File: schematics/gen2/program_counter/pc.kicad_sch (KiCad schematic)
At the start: 16 parts, among them J1 Bus_PCI_Express_x16, U1 74LS00, U2 74LS193, U3 74LS193, U4 74LS193, U5 74LS193, U6 74LS245, U7 74LS245

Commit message: pc and sp sch
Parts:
- removed C1, C2, C3, C4, C5, C6, C7, C8: C, Capacitor_THT:CP_Radial_D4.0mm_P1.50mm, symbol Device:C
- removed J1: Bus_PCI_Express_x16, Connector_PCBEdge:BUS_PCIexpress_x16, symbol Connector:Bus_PCI_Express_x16
- removed U1: 74LS00, Package_DIP:DIP-14_W7.62mm_Socket_LongPads, symbol 74xx:74LS00
- removed U2, U3, U4, U5: 74LS193, Package_DIP:DIP-16_W7.62mm_Socket_LongPads, symbol 74xx:74LS193
- removed U6, U7: 74LS245, Package_DIP:DIP-20_W7.62mm_Socket_LongPads, symbol 74xx:74LS245
- added BC1: BusConnector, Connector_PCBEdge:BUS_PCIexpress_x16, symbol cpu816symbols:BusConnector
- added C10, C11, C12, C13, C14, C15, C16, C9: C, Capacitor_THT:CP_Radial_D4.0mm_P1.50mm, symbol Device:C
- added U1: 74HC00, Package_DIP:DIP-14_W7.62mm_Socket_LongPads, symbol 74xx:74HC00
- added U2, U3, U4, U5: 74HC193, Package_DIP:DIP-16_W7.62mm_Socket_LongPads, symbol 74xx:74HC193
- added U6, U7: 74HC245, Package_DIP:DIP-20_W7.62mm_Socket_LongPads, symbol 74xx:74HC245
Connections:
- net CPu: now also U1.3, U4.5 (UP)
- net DH0: now also U2.3 (QA), U7.18 (B0)
- net DH1: now also U2.2 (QB), U7.17 (B1)
- net DH2: now also U2.6 (QC), U7.16 (B2)
- net DH3: now also U2.7 (QD), U7.15 (B3)
- net DH4: now also U3.3 (QA), U7.14 (B4)
- net DH5: now also U3.2 (QB), U7.13 (B5)
- net DH6: now also U3.6 (QC), U7.12 (B6)
- net DH7: now also U3.7 (QD), U7.11 (B7)
- net DL0: now also U4.3 (QA), U6.18 (B0)
- net DL1: now also U4.2 (QB), U6.17 (B1)
- net DL2: now also U4.6 (QC), U6.16 (B2)
- net DL3: now also U4.7 (QD), U6.15 (B3)
- net DL4: now also U5.3 (QA), U6.14 (B4)
- net DL5: now also U5.2 (QB), U6.13 (B5)
- net DL6: now also U5.6 (QC), U6.12 (B6)
- net DL7: now also U5.7 (QD), U6.11 (B7)
- net GND: now also BC1.A12 (GND), BC1.A13 (GND), BC1.A23 (GND), BC1.A32 (GND), BC1.A41 (GND), BC1.A50 (GND), BC1.A59 (GND), BC1.A63 (GND), BC1.A64 (GND), BC1.A65 (GND), BC1.A66 (GND), BC1.A70 (GND), BC1.A71 (GND), BC1.A72 (GND), BC1.A73 (GND), BC1.A74 (GND), BC1.A75 (GND), BC1.A76 (GND), BC1.B12 (GND), BC1.B13 (GND), BC1.B23 (GND), BC1.B32 (GND), BC1.B41 (GND), BC1.B50 (GND), BC1.B59 (GND), BC1.B62 (GND), BC1.B63 (GND), BC1.B64 (GND), BC1.B65 (GND), BC1.B66 (GND), BC1.B67 (GND), BC1.B68 (GND), BC1.B69 (GND), BC1.B70 (GND), BC1.B71 (GND), BC1.B72 (GND), BC1.B75 (GND), BC1.B76 (GND), C10.1, C11.1, C12.1, C13.1, C14.1, C15.2, C16.2, C9.2, U1.7 (GND), U2.8 (GND), U3.8 (GND), U4.8 (GND), U5.8 (GND), U6.1 (A->B), U6.10 (GND), U7.1 (A->B), U7.10 (GND)
- net PULSE: now also BC1.B74 (PULSE), U1.10, U1.13
- net Ph: now also U1.8, U2.11 (~{LOAD}), U3.11 (~{LOAD})
- net Pl: now also U1.11, U4.11 (~{LOAD}), U5.11 (~{LOAD})
- net VCC: now also BC1.A1 (VCC), BC1.A2 (VCC), BC1.A3 (VCC), BC1.A4 (VCC), BC1.A5 (VCC), BC1.B1 (VCC), BC1.B2 (VCC), BC1.B3 (VCC), BC1.B4 (VCC), BC1.B5 (VCC), C10.2, C11.2, C12.2, C13.2, C14.2, C15.1, C16.1, C9.1, U1.14 (VCC), U2.16 (VCC), U3.16 (VCC), U4.16 (VCC), U5.16 (VCC), U6.20 (VCC), U7.20 (VCC)
- new net: U2.12 (~{CO}), U3.5 (UP)
- new net: U2.13 (~{BO}), U3.4 (DOWN)
- new net: U2.4 (DOWN), U5.13 (~{BO})
- new net: U2.5 (UP), U5.12 (~{CO})
- new net: U4.12 (~{CO}), U5.5 (UP)
- new net: U4.13 (~{BO}), U5.4 (DOWN)
- new net DATA0: BC1.A51 (DATA0), U2.15 (A), U4.15 (A), U6.2 (A0), U7.2 (A0)
- new net DATA1: BC1.A52 (DATA1), U2.1 (B), U4.1 (B), U6.3 (A1), U7.3 (A1)
- new net DATA2: BC1.A53 (DATA2), U2.10 (C), U4.10 (C), U6.4 (A2), U7.4 (A2)
- new net DATA3: BC1.A54 (DATA3), U2.9 (D), U4.9 (D), U6.5 (A3), U7.5 (A3)
- new net DATA4: BC1.A55 (DATA4), U3.15 (A), U5.15 (A), U6.6 (A4), U7.6 (A4)
- new net DATA5: BC1.A56 (DATA5), U3.1 (B), U5.1 (B), U6.7 (A5), U7.7 (A5)
- new net DATA6: BC1.A57 (DATA6), U3.10 (C), U5.10 (C), U6.8 (A6), U7.8 (A6)
- new net DATA7: BC1.A58 (DATA7), U3.9 (D), U5.9 (D), U6.9 (A7), U7.9 (A7)
- new net LPCH: BC1.A17 (LPCH), U1.9
- new net LPCL: BC1.A18 (LPCL), U1.12
- new net PCINC: BC1.B47 (PCINC), U1.1
- new net RESET: BC1.A69 (RESET), U2.14 (CLR), U3.14 (CLR), U4.14 (CLR), U5.14 (CLR)
- new net ~{CLK}: BC1.B73 (~{CLK}), U1.2
- new net ~{RPCH}: BC1.B17 (~{RPCH}), U7.19 (CE)
- new net ~{RPCL}: BC1.B18 (~{RPCL}), U6.19 (CE)
- no-connect marks 4 -> 82

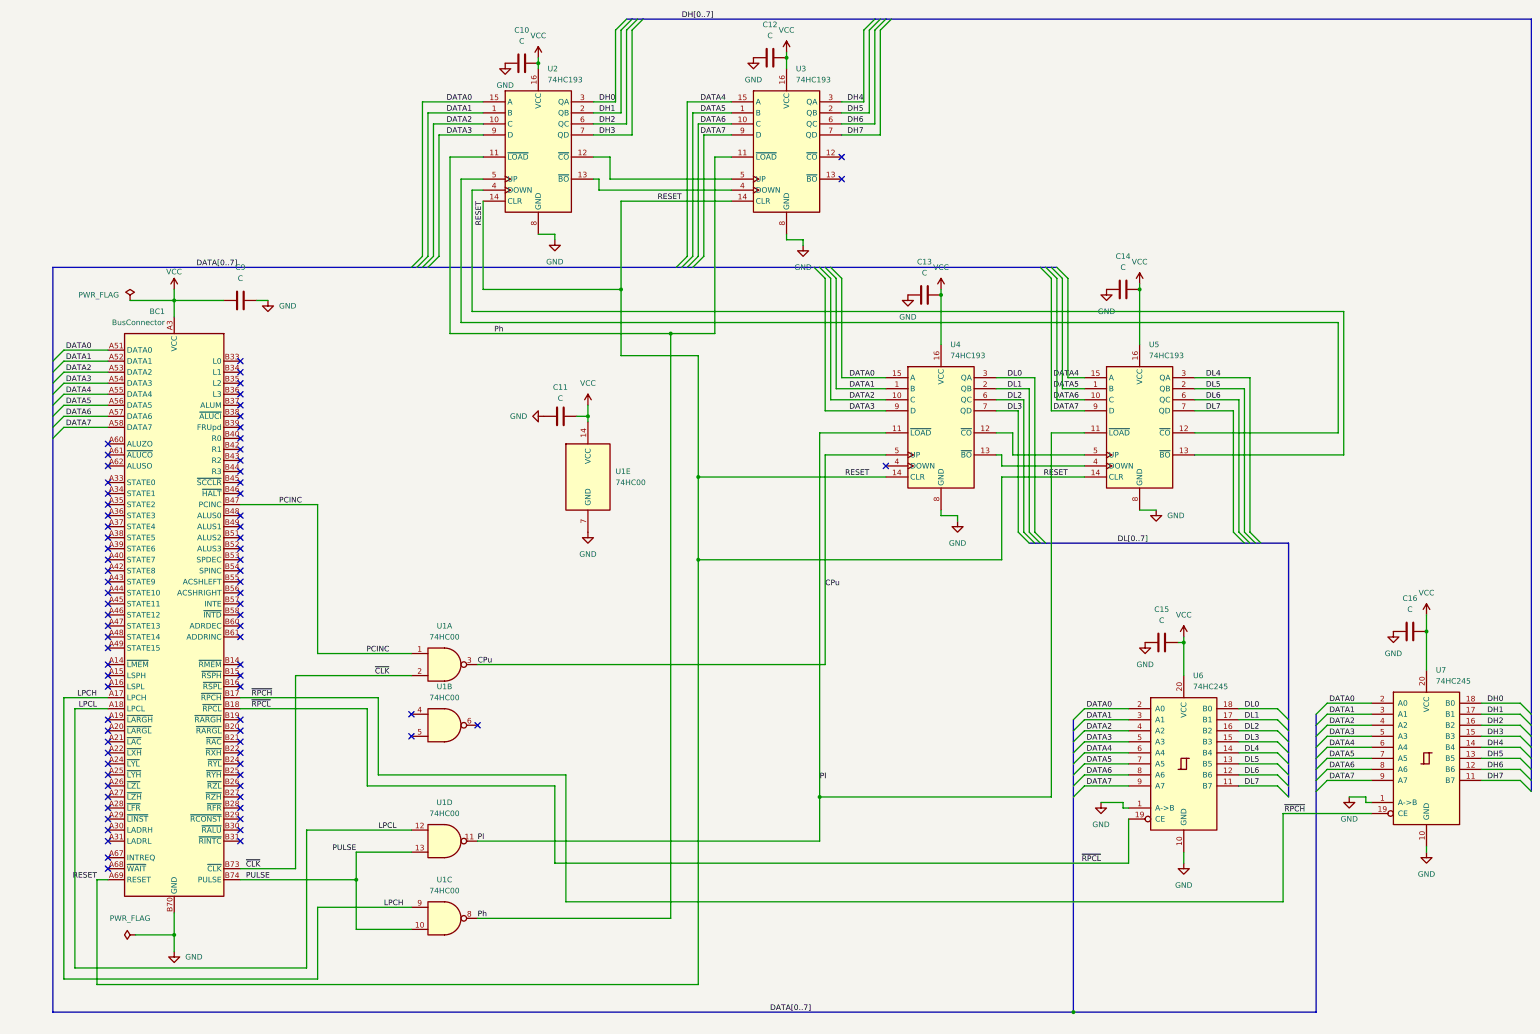
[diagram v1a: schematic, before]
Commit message: (feat) stack pointer and program counter pcb, QA needed.
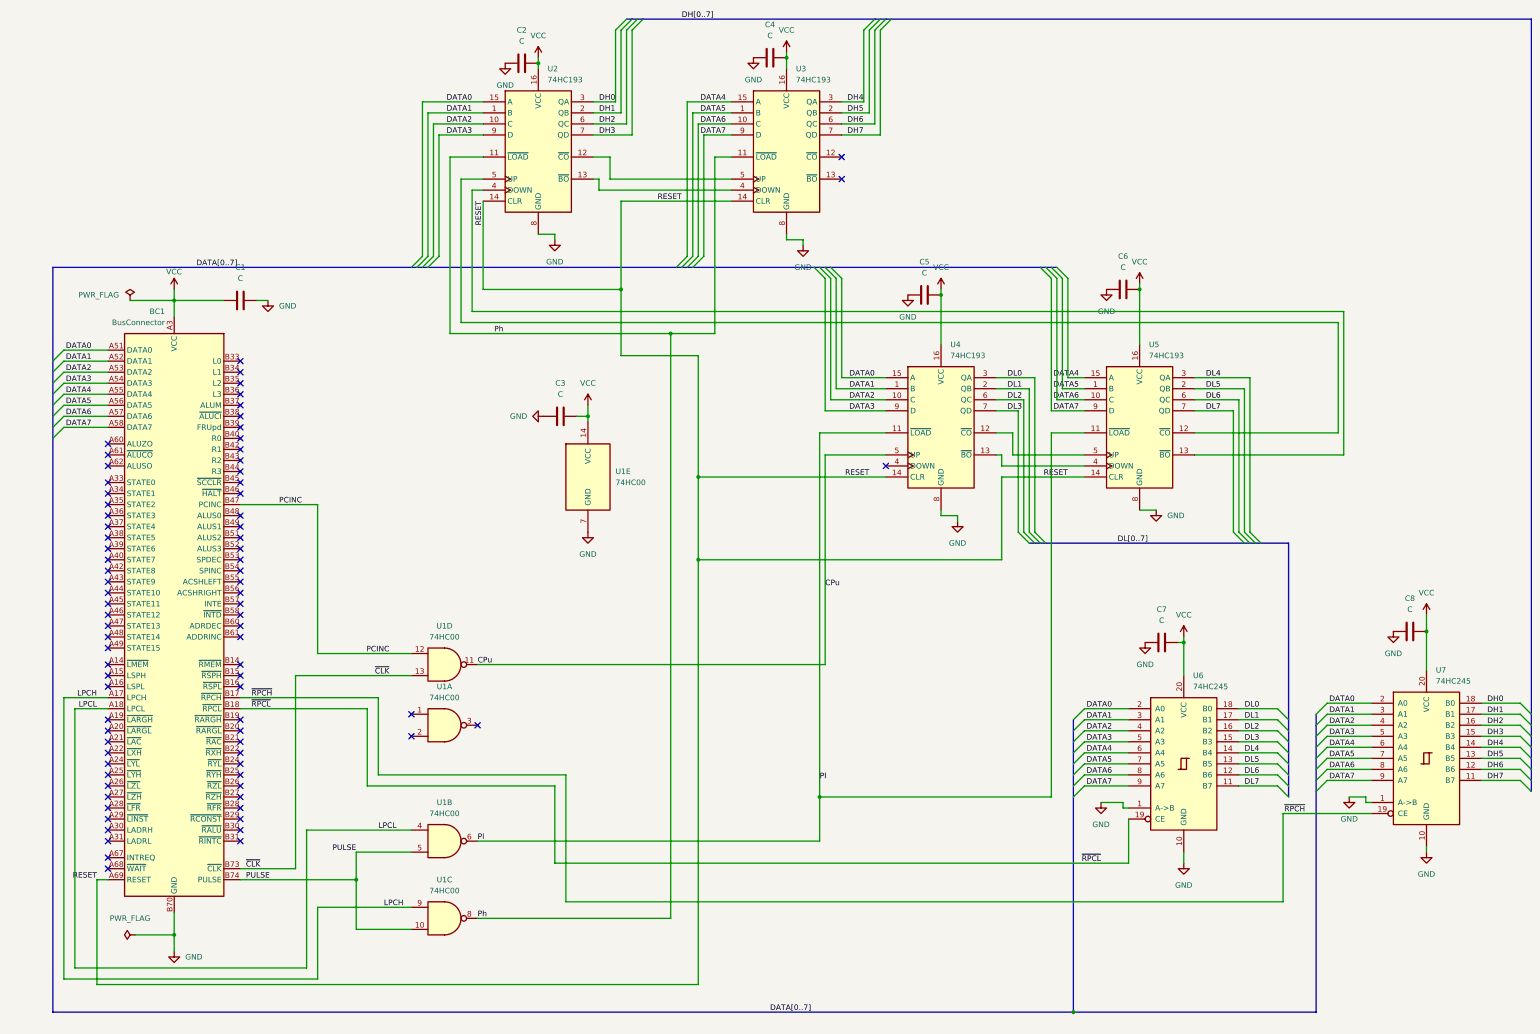
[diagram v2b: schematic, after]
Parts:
- C1: renamed from C9; footprint Capacitor_THT:CP_Radial_D4.0mm_P1.50mm -> Capacitor_SMD:C_0805_2012Metric_Pad1.18x1.45mm_HandSolder
- C2: renamed from C10; footprint Capacitor_THT:CP_Radial_D4.0mm_P1.50mm -> Capacitor_SMD:C_0805_2012Metric_Pad1.18x1.45mm_HandSolder
- C3: renamed from C11; footprint Capacitor_THT:CP_Radial_D4.0mm_P1.50mm -> Capacitor_SMD:C_0805_2012Metric_Pad1.18x1.45mm_HandSolder
- C4: renamed from C12; footprint Capacitor_THT:CP_Radial_D4.0mm_P1.50mm -> Capacitor_SMD:C_0805_2012Metric_Pad1.18x1.45mm_HandSolder
- C5: renamed from C13; footprint Capacitor_THT:CP_Radial_D4.0mm_P1.50mm -> Capacitor_SMD:C_0805_2012Metric_Pad1.18x1.45mm_HandSolder
- C6: renamed from C14; footprint Capacitor_THT:CP_Radial_D4.0mm_P1.50mm -> Capacitor_SMD:C_0805_2012Metric_Pad1.18x1.45mm_HandSolder
- C7: renamed from C15; footprint Capacitor_THT:CP_Radial_D4.0mm_P1.50mm -> Capacitor_SMD:C_0805_2012Metric_Pad1.18x1.45mm_HandSolder
- C8: renamed from C16; footprint Capacitor_THT:CP_Radial_D4.0mm_P1.50mm -> Capacitor_SMD:C_0805_2012Metric_Pad1.18x1.45mm_HandSolder
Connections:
- net CPu: now also U1.11; no longer U1.3
- net LPCL: now also U1.4; no longer U1.12
- net PCINC: now also U1.12; no longer U1.1
- net PULSE: now also U1.5; no longer U1.13
- net Pl: now also U1.6; no longer U1.11
- net ~{CLK}: now also U1.13; no longer U1.2

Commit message: program counter complete
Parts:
- added R1: R, Resistor_THT:R_Axial_DIN0207_L6.3mm_D2.5mm_P7.62mm_Horizontal, symbol Device:R
- C1: footprint Capacitor_SMD:C_0805_2012Metric_Pad1.18x1.45mm_HandSolder -> Capacitor_THT:C_Radial_D6.3mm_H5.0mm_P2.50mm
- C2, C3, C4, C5, C6, C7, C8: footprint Capacitor_SMD:C_0805_2012Metric_Pad1.18x1.45mm_HandSolder -> Capacitor_THT:C_Disc_D3.0mm_W1.6mm_P2.50mm
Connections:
- net VCC: now also R1.1
- net at U1.1: now also U1.2, R1.2
- no-connect marks 82 -> 80
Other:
- moved on the sheet: U1A
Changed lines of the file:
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@@
 	)
 	(junction
+		(at 147.32 179.07)
+		(diameter 0)
+		(color 0 0 0 0)
+	)
+	(junction
 		(at 222.25 196.85)
 		(diameter 0)
@@
 	)
 	(no_connect
-		(at 128.27 182.88)
-	)
-	(no_connect
 		(at 88.9 144.78)
 	)
@@
 	)
 	(no_connect
+		(at 170.18 181.61)
+	)
+	(no_connect
 		(at 58.42 201.93)
 	)
@@
 	)
 	(no_connect
-		(at 143.51 180.34)
-	)
-	(no_connect
 		(at 88.9 179.07)
 	)
@@
 	)
 	(no_connect
-		(at 128.27 177.8)
-	)
-	(no_connect
 		(at 227.33 49.53)
 	)
@@
 	(wire
 		(pts
+			(xy 147.32 179.07) (xy 154.94 179.07)
+		)
+		(stroke
+			(width 0)
+			(type default)
+		)
+	)
+	(wire
+		(pts
 			(xy 194.31 142.24) (xy 264.16 142.24)
 		)
@@
 	(wire
 		(pts
+			(xy 147.32 179.07) (xy 147.32 184.15)
+		)
+		(stroke
+			(width 0)
+			(type default)
+		)
+	)
+	(wire
+		(pts
 			(xy 157.48 27.94) (xy 157.48 29.21)
 		)
@@
 		)
 	)
+	(wire
+		(pts
+			(xy 137.16 179.07) (xy 134.62 179.07)
+		)
+		(stroke
+			(width 0)
+			(type default)
+		)
+	)
 	(bus
 		(pts
@@
 	(wire
 		(pts
+			(xy 144.78 179.07) (xy 147.32 179.07)
+		)
+		(stroke
+			(width 0)
+			(type default)
+		)
+	)
+	(wire
+		(pts
 			(xy 55.88 215.9) (xy 58.42 215.9)
 		)
@@
 	(wire
 		(pts
+			(xy 147.32 184.15) (xy 154.94 184.15)
+		)
+		(stroke
+			(width 0)
+			(type default)
+		)
+	)
+	(wire
+		(pts
 			(xy 106.68 222.25) (xy 128.27 222.25)
 		)
@@
 	)
 	(symbol
+		(lib_id "power:VCC")
+		(at 134.62 179.07 0)
+		(unit 1)
+		(exclude_from_sim no)
+		(in_bom yes)
+		(on_board yes)
+		(dnp no)
+		(fields_autoplaced yes)
+		(property "Reference" "#PWR01"
+			(at 134.62 182.88 0)
+			(effects
+				(font
+					(size 1.27 1.27)
+				)
+				(hide yes)
+			)
+		)
+		(property "Value" "VCC"
+			(at 134.62 173.99 0)
+			(effects
+				(font
+					(size 1.27 1.27)
+				)
+			)
+		)
+		(property "Footprint" ""
+			(at 134.62 179.07 0)
+			(effects
+				(font
+					(size 1.27 1.27)
+				)
+				(hide yes)
+			)
+		)
+		(property "Datasheet" ""
+			(at 134.62 179.07 0)
+			(effects
+				(font
+					(size 1.27 1.27)
+				)
+				(hide yes)
+			)
+		)
+		(property "Description" "Power symbol creates a global label with name \"VCC\""
+			(at 134.62 179.07 0)
+			(effects
+				(font
+					(size 1.27 1.27)
+				)
+				(hide yes)
+			)
+		)
+		(pin "1"
+		)
+		(instances
+			(project ""
+				(path "/34f7239d-5890-443b-b0ee-b6e214f6aaae"
+					(reference "#PWR01")
+					(unit 1)
+				)
+			)
+		)
+	)
+	(symbol
 		(lib_id "74xx:74HC245")
 		(at 361.95 187.96 0)
@@
 			)
 		)
-		(property "Footprint" "Capacitor_SMD:C_0805_2012Metric_Pad1.18x1.45mm_HandSolder"
+		(property "Footprint" "Capacitor_THT:C_Disc_D3.0mm_W1.6mm_P2.50mm"
 			(at 250.19 80.3148 0)
 			(effects
@@
 			)
 		)
-		(property "Footprint" "Capacitor_SMD:C_0805_2012Metric_Pad1.18x1.45mm_HandSolder"
+		(property "Footprint" "Capacitor_THT:C_Disc_D3.0mm_W1.6mm_P2.50mm"
 			(at 214.63 25.7048 0)
 			(effects
@@
 			)
 		)
-		(property "Footprint" "Capacitor_SMD:C_0805_2012Metric_Pad1.18x1.45mm_HandSolder"
+		(property "Footprint" "Capacitor_THT:C_Disc_D3.0mm_W1.6mm_P2.50mm"
 			(at 166.37 108.2548 0)
 			(effects
@@
 	(symbol
 		(lib_id "74xx:74HC00")
-		(at 135.89 180.34 0)
+		(at 162.56 181.61 0)
 		(unit 1)
 		(exclude_from_sim no)
@@
 		(fields_autoplaced yes)
 		(property "Reference" "U1"
-			(at 135.8817 171.45 0)
+			(at 162.5517 172.72 0)
 			(effects
 				(font
@@
 		)
 		(property "Value" "74HC00"
-			(at 135.8817 173.99 0)
+			(at 162.5517 175.26 0)
 			(effects
 				(font
@@
 		)
 		(property "Footprint" "Package_DIP:DIP-14_W7.62mm_Socket_LongPads"
-			(at 135.89 180.34 0)
+			(at 162.56 181.61 0)
 			(effects
 				(font
@@
 		)
 		(property "Datasheet" "http://www.ti.com/lit/gpn/sn74hc00"
-			(at 135.89 180.34 0)
+			(at 162.56 181.61 0)
 			(effects
 				(font
@@
 		)
 		(property "Description" "quad 2-input NAND gate"
-			(at 135.89 180.34 0)
+			(at 162.56 181.61 0)
 			(effects
 				(font
@@
 			)
 		)
-		(property "Footprint" "Capacitor_SMD:C_0805_2012Metric_Pad1.18x1.45mm_HandSolder"
+		(property "Footprint" "Capacitor_THT:C_Disc_D3.0mm_W1.6mm_P2.50mm"
 			(at 354.33 159.7152 0)
 			(effects
@@
 			)
 		)
-		(property "Footprint" "Capacitor_SMD:C_0805_2012Metric_Pad1.18x1.45mm_HandSolder"
+		(property "Footprint" "Capacitor_THT:C_Radial_D6.3mm_H5.0mm_P2.50mm"
 			(at 92.71 83.5152 0)
 			(effects
@@
 			)
 		)
-		(property "Footprint" "Capacitor_SMD:C_0805_2012Metric_Pad1.18x1.45mm_HandSolder"
+		(property "Footprint" "Capacitor_THT:C_Disc_D3.0mm_W1.6mm_P2.50mm"
 			(at 157.48 26.9748 0)
 			(effects
@@
 	)
 	(symbol
+		(lib_id "Device:R")
+		(at 140.97 179.07 90)
+		(unit 1)
+		(exclude_from_sim no)
+		(in_bom yes)
+		(on_board yes)
+		(dnp no)
+		(fields_autoplaced yes)
+		(property "Reference" "R1"
+			(at 140.97 172.72 90)
+			(effects
+				(font
+					(size 1.27 1.27)
+				)
+			)
+		)
+		(property "Value" "R"
+			(at 140.97 175.26 90)
+			(effects
+				(font
+					(size 1.27 1.27)
+				)
+			)
+		)
+		(property "Footprint" "Resistor_THT:R_Axial_DIN0207_L6.3mm_D2.5mm_P7.62mm_Horizontal"
+			(at 140.97 180.848 90)
+			(effects
+				(font
+					(size 1.27 1.27)
+				)
+				(hide yes)
+			)
+		)
+		(property "Datasheet" "~"
+			(at 140.97 179.07 0)
+			(effects
+				(font
+					(size 1.27 1.27)
+				)
+				(hide yes)
+			)
+		)
+		(property "Description" "Resistor"
+			(at 140.97 179.07 0)
+			(effects
+				(font
+					(size 1.27 1.27)
+				)
+				(hide yes)
+			)
+		)
+		(pin "2"
+		)
+		(pin "1"
+		)
+		(instances
+			(project ""
+				(path "/34f7239d-5890-443b-b0ee-b6e214f6aaae"
+					(reference "R1")
+					(unit 1)
+				)
+			)
+		)
+	)
+	(symbol
 		(lib_id "74xx:74HC00")
 		(at 135.89 166.37 0)
@@
 			)
 		)
-		(property "Footprint" "Capacitor_SMD:C_0805_2012Metric_Pad1.18x1.45mm_HandSolder"
+		(property "Footprint" "Capacitor_THT:C_Disc_D3.0mm_W1.6mm_P2.50mm"
 			(at 297.18 162.2552 0)
 			(effects
@@
 			)
 		)
-		(property "Footprint" "Capacitor_SMD:C_0805_2012Metric_Pad1.18x1.45mm_HandSolder"
+		(property "Footprint" "Capacitor_THT:C_Disc_D3.0mm_W1.6mm_P2.50mm"
 			(at 295.91 79.0448 0)
 			(effects

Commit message: fix(pc): changed resistor, capacitors footprints
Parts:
- C2, C3, C4, C5, C6, C7, C8: footprint Capacitor_THT:C_Disc_D3.0mm_W1.6mm_P2.50mm -> Capacitor_THT:C_Disc_D5.0mm_W2.5mm_P5.00mm
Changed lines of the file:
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@@
 			)
 		)
-		(property "Footprint" "Capacitor_THT:C_Disc_D3.0mm_W1.6mm_P2.50mm"
+		(property "Footprint" "Capacitor_THT:C_Disc_D5.0mm_W2.5mm_P5.00mm"
 			(at 250.19 80.3148 0)
 			(effects
@@
 			)
 		)
-		(property "Footprint" "Capacitor_THT:C_Disc_D3.0mm_W1.6mm_P2.50mm"
+		(property "Footprint" "Capacitor_THT:C_Disc_D5.0mm_W2.5mm_P5.00mm"
 			(at 214.63 25.7048 0)
 			(effects
@@
 			)
 		)
-		(property "Footprint" "Capacitor_THT:C_Disc_D3.0mm_W1.6mm_P2.50mm"
+		(property "Footprint" "Capacitor_THT:C_Disc_D5.0mm_W2.5mm_P5.00mm"
 			(at 166.37 108.2548 0)
 			(effects
@@
 			)
 		)
-		(property "Footprint" "Capacitor_THT:C_Disc_D3.0mm_W1.6mm_P2.50mm"
+		(property "Footprint" "Capacitor_THT:C_Disc_D5.0mm_W2.5mm_P5.00mm"
 			(at 354.33 159.7152 0)
 			(effects
@@
 			)
 		)
-		(property "Footprint" "Capacitor_THT:C_Disc_D3.0mm_W1.6mm_P2.50mm"
+		(property "Footprint" "Capacitor_THT:C_Disc_D5.0mm_W2.5mm_P5.00mm"
 			(at 157.48 26.9748 0)
 			(effects
@@
 			)
 		)
-		(property "Footprint" "Capacitor_THT:C_Disc_D3.0mm_W1.6mm_P2.50mm"
+		(property "Footprint" "Capacitor_THT:C_Disc_D5.0mm_W2.5mm_P5.00mm"
 			(at 297.18 162.2552 0)
 			(effects
@@
 			)
 		)
-		(property "Footprint" "Capacitor_THT:C_Disc_D3.0mm_W1.6mm_P2.50mm"
+		(property "Footprint" "Capacitor_THT:C_Disc_D5.0mm_W2.5mm_P5.00mm"
 			(at 295.91 79.0448 0)
 			(effects
